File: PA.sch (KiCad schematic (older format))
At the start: 34 parts, among them J7 RF_Shield_One_Piece, U5 CC1190

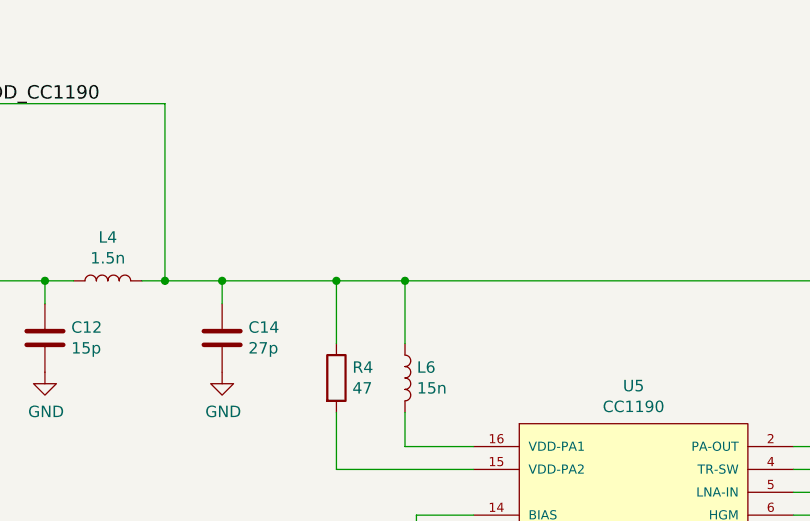
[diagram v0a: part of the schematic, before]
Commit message: Fixed (most) pwr flag issues
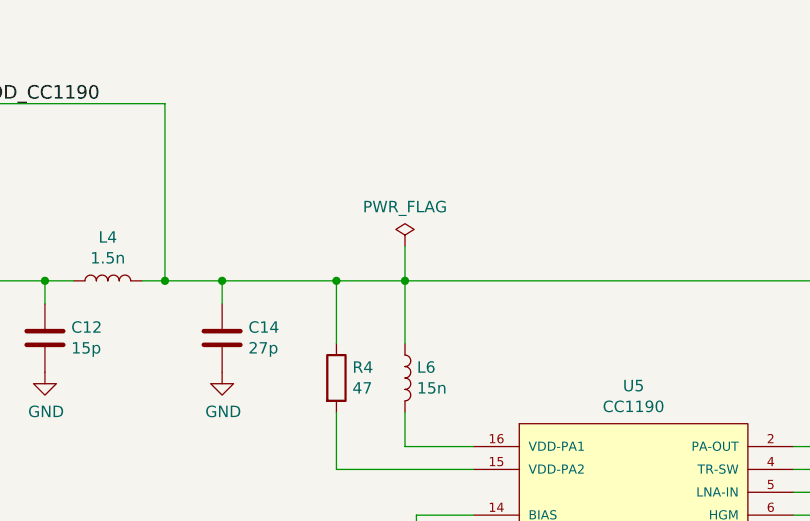
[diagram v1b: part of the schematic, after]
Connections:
- wire segments 103 -> 104
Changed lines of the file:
@@
 	1    0    0    -1
 $EndComp
+$Comp
+L power:PWR_FLAG #FLG0104
+U 1 1 602F1027
+P 5050 1600
+F 0 "#FLG0104" H 5050 1675 50  0001 C CNN
+F 1 "PWR_FLAG" H 5050 1773 50  0000 C CNN
+F 2 "" H 5050 1600 50  0001 C CNN
+F 3 "~" H 5050 1600 50  0001 C CNN
+	1    5050 1600
+	1    0    0    -1
+$EndComp
+Wire Wire Line
+	5050 1600 5050 1750
 $EndSCHEMATC
